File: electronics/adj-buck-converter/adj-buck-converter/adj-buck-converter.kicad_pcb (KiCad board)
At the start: 2 copper layers, 11 parts, among them J1 24v-INPUT, J2 ADJ_OUTPUT, U1 LM2596S-ADJ

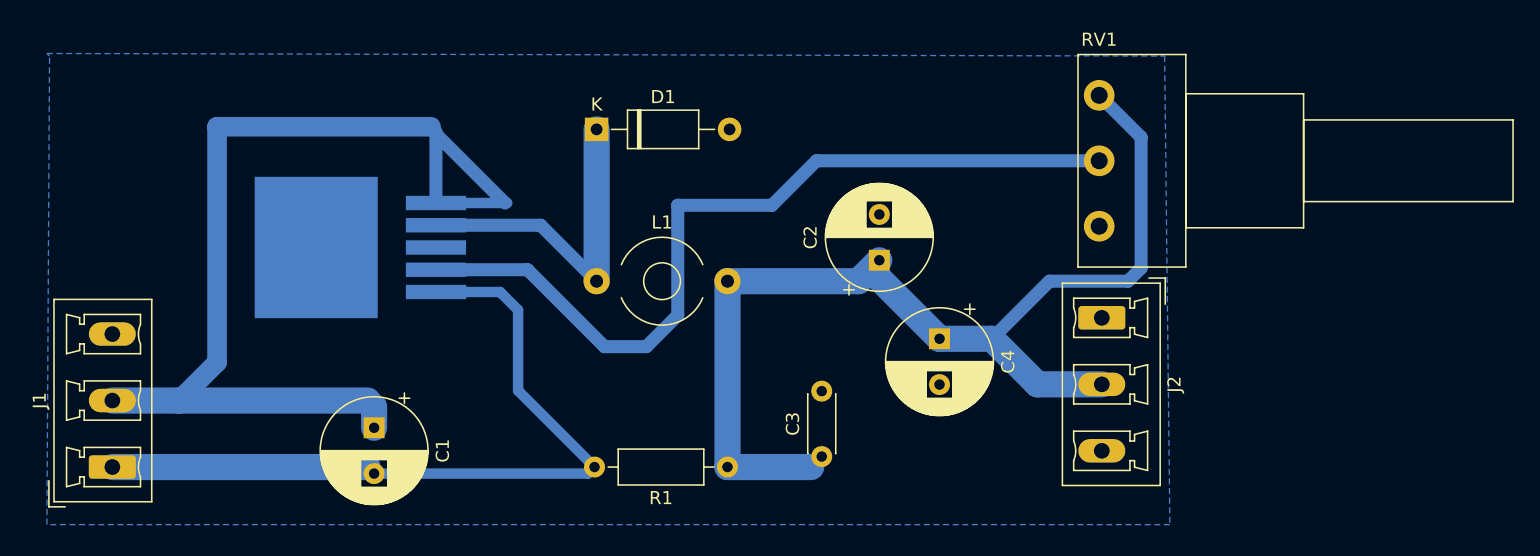
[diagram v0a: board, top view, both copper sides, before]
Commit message: Smaller potentiometer tracks
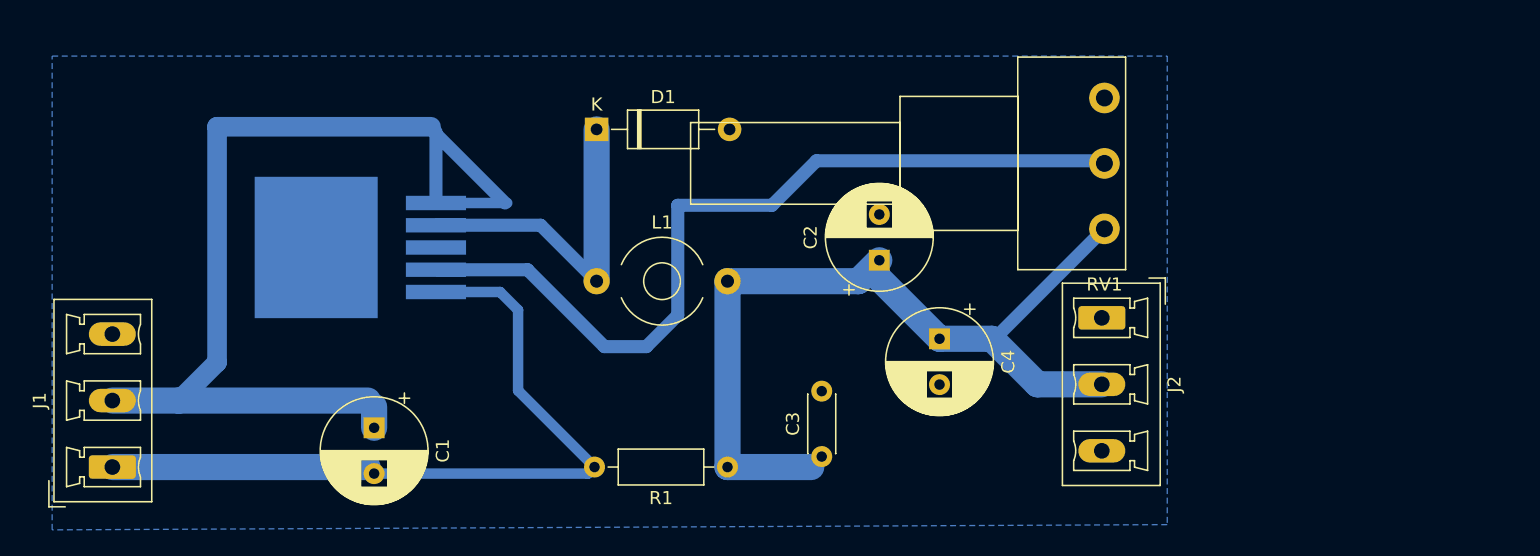
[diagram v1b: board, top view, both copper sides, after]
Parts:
- moved RV1 9.81 mm to (118.8, 39.8), turned to 180 degrees
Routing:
- net Net-(C2-Pad1): track 83.9 -> 71.8 mm
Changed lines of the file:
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@@
     (thickness 1.6)
     (drawings 0)
-    (tracks 44)
+    (tracks 42)
     (zones 0)
     (modules 11)
@@
   (page A4)
   (layers
-    (0 F.Cu signal hide)
+    (0 F.Cu signal)
     (31 B.Cu signal)
     (32 B.Adhes user)
@@
   )
   (module Potentiometer_THT:Potentiometer_Piher_PC-16_Single_Horizontal (layer F.Cu)
-    (at 118.4 49.6)
+    (at 118.8 39.8 180)
     (descr "Potentiometer, horizontal, Piher PC-16 Single, http://www.piher-nacesa.com/pdf/20-PC16v03.pdf")
     (tags "Potentiometer horizontal Piher PC-16 Single")
@@
     (fp_line (start -1.5 3) (end 6.5 3) (layer F.Fab) (width 0.1))
     (fp_line (start -1.5 -13) (end -1.5 3) (layer F.Fab) (width 0.1))
-    (pad 1 thru_hole circle (at 0 0) (size 2.34 2.34) (drill 1.3) (layers *.Cu *.Mask)
+    (pad 1 thru_hole circle (at 0 0 180) (size 2.34 2.34) (drill 1.3) (layers *.Cu *.Mask)
       (net 1 GND))
-    (pad 2 thru_hole circle (at 0 -5) (size 2.34 2.34) (drill 1.3) (layers *.Cu *.Mask)
+    (pad 2 thru_hole circle (at 0 -5 180) (size 2.34 2.34) (drill 1.3) (layers *.Cu *.Mask)
       (net 5 "Net-(RV1-Pad2)"))
-    (pad 3 thru_hole circle (at 0 -10) (size 2.34 2.34) (drill 1.3) (layers *.Cu *.Mask)
+    (pad 3 thru_hole circle (at 0 -10 180) (size 2.34 2.34) (drill 1.3) (layers *.Cu *.Mask)
       (net 3 "Net-(C2-Pad1)"))
     (model ${KISYS3DMOD}/Potentiometer_THT.3dshapes/Potentiometer_Piher_PC-16_Single_Horizontal.wrl
@@
   (segment (start 96.4 68) (end 97.2 67.2) (width 0.8) (layer B.Cu) (net 3))
   (segment (start 90 68) (end 96.4 68) (width 2) (layer B.Cu) (net 3))
-  (segment (start 118.4 39.6) (end 121.6 42.8) (width 1) (layer B.Cu) (net 3))
-  (segment (start 121.6 42.8) (end 121.6 52.8) (width 1) (layer B.Cu) (net 3))
-  (segment (start 121.6 52.8) (end 120.6 53.8) (width 1) (layer B.Cu) (net 3))
-  (segment (start 114.6 53.8) (end 110.2 58.2) (width 1) (layer B.Cu) (net 3))
-  (segment (start 120.6 53.8) (end 114.6 53.8) (width 1) (layer B.Cu) (net 3))
   (segment (start 90 53.8) (end 90 68) (width 2) (layer B.Cu) (net 3))
   (segment (start 100 53.8) (end 101.6 52.2) (width 2) (layer B.Cu) (net 3))
@@
   (segment (start 101.6 53.6) (end 106.2 58.2) (width 2) (layer B.Cu) (net 3))
   (segment (start 101.6 52.2) (end 101.6 53.6) (width 1) (layer B.Cu) (net 3))
+  (segment (start 108 58.2) (end 106.2 58.2) (width 1) (layer B.Cu) (net 3))
+  (segment (start 110.4 58.2) (end 108 58.2) (width 1) (layer B.Cu) (net 3))
+  (segment (start 118.8 49.8) (end 110.4 58.2) (width 1) (layer B.Cu) (net 3))
   (segment (start 75.725 49.525) (end 80 53.8) (width 1) (layer B.Cu) (net 4))
   (segment (start 67.725 49.525) (end 75.725 49.525) (width 1) (layer B.Cu) (net 4))
@@
     (polygon
       (pts
-        (xy 38 36.4) (xy 123.4 36.6) (xy 123.8 72.4) (xy 38 72.4) (xy 38.2 36.6)
+        (xy 38.4 36.6) (xy 123.6 36.6) (xy 123.6 72.4) (xy 38.4 72.8)
       )
     )
